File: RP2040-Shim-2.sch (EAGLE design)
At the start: 43 parts, among them SW1 KMR2, U1 RP2040_QFN56, U2 2MB Flash, U3 AP2112-3.3, U4 PMS150C-6PIN, Y1 12MHZ

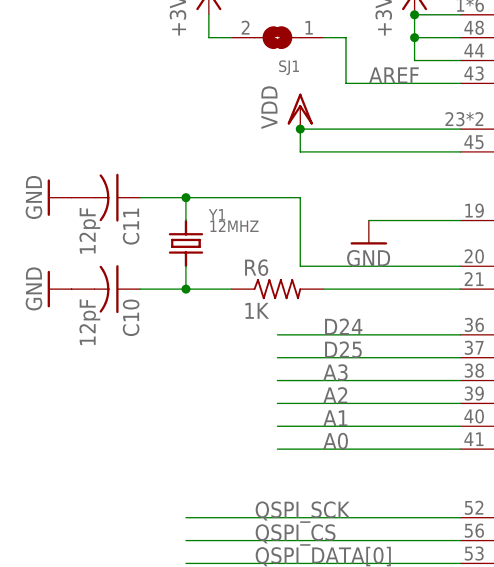
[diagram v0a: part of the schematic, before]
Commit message: Update osc caps to 15 pF, add pinout diagram
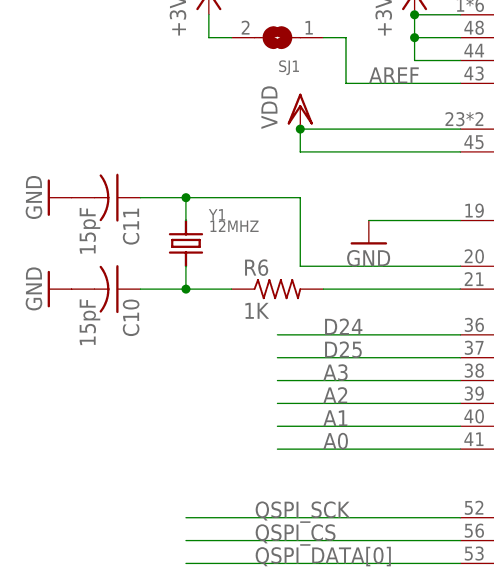
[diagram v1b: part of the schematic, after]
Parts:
- C10, C11: value 12pF -> 15pF
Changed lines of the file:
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@@
 <part name="C2" library="rcl" deviceset="C-US" device="C0805K" value="22uF"/>
 <part name="R1" library="rcl" deviceset="R-US_" device="R0402" value="10K"/>
-<part name="C11" library="rcl" deviceset="C-US" device="C0402K" value="12pF"/>
-<part name="C10" library="rcl" deviceset="C-US" device="C0402K" value="12pF"/>
+<part name="C11" library="rcl" deviceset="C-US" device="C0402K" value="15pF"/>
+<part name="C10" library="rcl" deviceset="C-US" device="C0402K" value="15pF"/>
 <part name="R2" library="rcl" deviceset="R-US_" device="R0402" value="10K"/>
 <part name="R5" library="rcl" deviceset="R-US_" device="R0402" value="2.2K"/>
